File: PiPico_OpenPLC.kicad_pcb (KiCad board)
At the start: 2 copper layers, 155.6 x 86 mm, 196 parts, among them J1 5 Pin 3.5mm, J10 Conn_01x03_Male, J11 Conn_01x03_Male, J12 5 Pin 3.5mm, J2 5 Pin 3.5mm, J3 5 Pin 3.5mm, J4 5 Pin 3.5mm, J5 5 Pin 3.5mm, J6 5 Pin 3.5mm, J7 5 Pin 3.5mm, J8 5 Pin 3.5mm, J9 Conn_01x06_Male, K1 HF32F/xxx-Z, K2 HF32F/xxx-Z, K3 HF32F/xxx-Z, K4 HF32F/xxx-Z, Q1 MMBT2222A 1P, SW1 TS1187, U1 Pico, U10 ULN2803A, U11 LM2596S-12, U2 AMS1117-5.0, U3 LM4040DBZ-3, U4 LM358, U5 LM358, U6 LM358, U7 74HC14, U8 ULN2803A, U9 ULN2803A

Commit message: routed version
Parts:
- JP1, JP2, JP3, JP4, JP5, NT1, NT2, NT3, NT4, NT5, NT6: moved to B.Cu
- moved C11 242.3 mm to (38.6, 77.6), turned to 90 degrees
- moved JP3 238.9 mm to (42.1, 69.9), turned to 90 degrees
- moved D7 238.5 mm to (42.7, 44.1), turned to 90 degrees
- moved C1 237.4 mm to (38.6, 63.2), turned to 90 degrees
- moved C4 237.3 mm to (39.7, 80.4), turned to 180 degrees
- moved C3 237.0 mm to (39.7, 84.3), turned to -90 degrees
- moved C8 235.8 mm to (40.3, 77.6), turned to 90 degrees
- moved JP4 234.9 mm to (46.7, 55.6)
- moved D10 234.9 mm to (46.2, 44.1), turned to 90 degrees
- moved JP2 234.4 mm to (46.7, 58.5)
- moved D43 231.2 mm to (49.7, 44.1), turned to 90 degrees
- moved D9 230.9 mm to (45.6, 63.2), turned to -90 degrees
- moved C2 229.7 mm to (45.6, 67.1)
- moved F10 228.6 mm to (59.0, 36.5), turned to 180 degrees
- moved D44 227.7 mm to (53.2, 44.1), turned to 90 degrees
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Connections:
- net Vdrive renamed VPP
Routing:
- net GND: track 0.00 -> 898.8 mm, vias 0 -> 10
- net VCC: track 0.00 -> 298.8 mm, vias 0 -> 4
- net GNDA: track 0.00 -> 222.0 mm, vias 0 -> 6
- net VCCQ: track 0.00 -> 206.4 mm, vias 0 -> 2
- net VPP: track 0.00 -> 188.2 mm
- net +3V3: track 0.00 -> 171.9 mm, vias 0 -> 1
- net /PWMo0: track 0.00 -> 171.4 mm, vias 0 -> 2
- net VBUS: track 0.00 -> 141.5 mm, vias 0 -> 2
- net /Di0: track 0.00 -> 129.6 mm
- net /PWMo1: track 0.00 -> 121.4 mm, vias 0 -> 1
- net ADC_VREF: track 0.00 -> 116.6 mm, vias 0 -> 1
- net +12V: track 0.00 -> 103.8 mm, vias 0 -> 3
- net /Di7: track 0.00 -> 103.4 mm
- net /Di2: track 0.00 -> 103.3 mm, vias 0 -> 2
- net +5V: track 0.00 -> 93.6 mm, vias 0 -> 2
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
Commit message: snap
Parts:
- added C46: 50V 100nF X7R, Capacitor_SMD:C_0603_1608Metric, F.Cu at (109.7, 97.4)
- added C47: 50V 100nF X7R, Capacitor_SMD:C_0603_1608Metric, F.Cu at (78.2, 88.3)
- added C48: 50V 100nF X7R, Capacitor_SMD:C_0603_1608Metric, F.Cu at (119.9, 64.9)
- added D46: Red, LED_SMD:LED_0603_1608Metric, F.Cu at (49.7, 110.0)
- added D47: Red, LED_SMD:LED_0603_1608Metric, F.Cu at (46.2, 110.0)
- added D48: Red, LED_SMD:LED_0603_1608Metric, F.Cu at (42.7, 110.0)
- added D49: Red, LED_SMD:LED_0603_1608Metric, F.Cu at (39.2, 110.0)
- added J13: Conn_01x06_Male, Connector_PinHeader_2.54mm:PinHeader_1x06_P2.54mm_Vertical, F.Cu at (38.0, 97.6)
- added J14: 5 Pin 3.5mm, Connector_Phoenix_MC:PhoenixContact_MC_1,5_5-G-3.5_1x05_P3.50mm_Horizontal, F.Cu at (39.2, 114.8)
- added J15: Conn_01x06_Male, Connector_PinHeader_2.54mm:PinHeader_1x06_P2.54mm_Vertical, F.Cu at (183.8, 55.6)
- added J16: Conn_01x06_Male, Connector_PinHeader_2.54mm:PinHeader_1x06_P2.54mm_Vertical, F.Cu at (109.2, 73.8)
- added J17: Conn_01x06_Male, Connector_PinHeader_2.54mm:PinHeader_1x06_P2.54mm_Vertical, F.Cu at (109.2, 92.2)
- added J18: Conn_01x06_Male, Connector_PinHeader_2.54mm:PinHeader_1x06_P2.54mm_Vertical, F.Cu at (113.2, 61.1)
- added J19: Conn_01x06_Male, Connector_PinHeader_2.54mm:PinHeader_1x06_P2.54mm_Vertical, F.Cu at (113.2, 79.5)
- added J20: Conn_01x06_Male, Connector_PinHeader_2.54mm:PinHeader_1x06_P2.54mm_Vertical, F.Cu at (73.4, 43.2)
- added J21: Conn_01x06_Male, Connector_PinHeader_2.54mm:PinHeader_1x06_P2.54mm_Vertical, F.Cu at (148.2, 110.0)
- added J22: 5 Pin 3.5mm, Connector_Phoenix_MC:PhoenixContact_MC_1,5_5-G-3.5_1x05_P3.50mm_Horizontal, F.Cu at (148.2, 114.8)
- added JP8: SolderJumper_3_Bridged12, Connector_PinHeader_2.54mm:PinHeader_1x03_P2.54mm_Vertical, F.Cu at (139.9, 101.4)
- added NT7: NetTie_2, NetTie:NetTie-2_SMD_Pad0.5mm, B.Cu at (112.2, 97.4)
- added NT8: NetTie_2, NetTie:NetTie-2_SMD_Pad0.5mm, B.Cu at (121.4, 65.2)
- added NT9: NetTie_2, NetTie:NetTie-2_SMD_Pad0.5mm, B.Cu at (76.5, 80.0)
- added R45: 100k, Resistor_SMD:R_0603_1608Metric, F.Cu at (47.9, 110.0)
- added R46: 100k, Resistor_SMD:R_0603_1608Metric, F.Cu at (44.4, 110.0)
- added R47: 100k, Resistor_SMD:R_0603_1608Metric, F.Cu at (40.9, 110.0)
- added R48: 100k, Resistor_SMD:R_0603_1608Metric, F.Cu at (37.4, 110.0)
- added RN7: 470, Resistor_SMD:R_Array_Convex_4x0603, F.Cu at (50.8, 104.3)
- added U12: PCF8574, Package_SO:SOIC-16W_7.5x10.3mm_P1.27mm, F.Cu at (116.7, 101.4)
- added U15: PCF8574, Package_SO:SOIC-16W_7.5x10.3mm_P1.27mm, F.Cu at (126.9, 69.2)
- added U16: PCF8574, Package_SO:SOIC-16W_7.5x10.3mm_P1.27mm, F.Cu at (71.8, 84.3)
- J9: value Conn_01x06_Male -> 5 Pin 3.5mm; footprint Connector_PinHeader_2.54mm:PinHeader_1x06_P2.54mm_Vertical -> Connector_Phoenix_MC:PhoenixContact_MC_1,5_5-G-3.5_1x05_P3.50mm_Horizontal
- moved U10 62.5 mm to (46.7, 92.9), turned to 180 degrees
- moved C45 29.1 mm to (106.8, 105.1), turned to 180 degrees
- moved C44 28.1 mm to (106.8, 103.4), turned to 0 degrees
- moved J11 27.5 mm to (89.1, 88.1), turned to 90 degrees
- moved F8 26.4 mm to (106.8, 98.1), turned to -90 degrees
- moved RN6 25.1 mm to (107.4, 110.0), turned to 0 degrees
- moved D5 24.9 mm to (71.0, 63.4), turned to 90 degrees
- moved D4 24.7 mm to (75.0, 63.4), turned to 90 degrees
- moved J12 24.0 mm to (63.1, 114.8)
- moved J8 23.4 mm to (83.5, 114.8)
- moved C10 21.7 mm to (59.4, 87.7)
- moved C41 21.7 mm to (57.5, 87.7)
- moved D8 21.7 mm to (57.5, 79.5)
- moved F3 21.7 mm to (57.5, 84.7)
- moved C7 21.7 mm to (61.3, 85.9)
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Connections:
- F9 pad 1: VPP -> Net-(JP8-C)
- J9 pad 1: +3V3 -> Net-(J20-Pin_1)
- J9 pad 2: /SDA / UART Tx / SPI Rx -> Net-(J20-Pin_2)
- J9 pad 3: /SCL / UART Rx / SPI ~{CS} -> Net-(J20-Pin_3)
- J9 pad 4: /SPI SCK -> Net-(J20-Pin_4)
- J9 pad 5: /SPI Tx -> Net-(J20-Pin_5)
- R14 pad 1: GNDA -> GND
- R15 pad 1: GNDA -> GND
- U1 pad 1: /SDA / UART Tx / SPI Rx -> /UART0_TX
- U1 pad 10: /Di1 -> unconnected-(U1-GPIO7-Pad10)
- U1 pad 11: /Di2 -> /UART1_TX
- U1 pad 12: /Di3 -> /UART1_RX
- U1 pad 14: /Di4 -> unconnected-(U1-GPIO10-Pad14)
- U1 pad 15: /Di5 -> unconnected-(U1-GPIO11-Pad15)
- U1 pad 16: /Di6 -> /SPI1_RX
- U1 pad 17: /Di7 -> /SPI1_CSn
- U1 pad 19: /Do0 -> /SPI1_SCK
- U1 pad 2: /SCL / UART Rx / SPI ~{CS} -> /UART0_RX
- U1 pad 20: /Do1 -> /SPI1_TX
- U1 pad 21: /Do2 -> /SPI0_RX
- U1 pad 22: /Do3 -> /SPI0_CSn
- U1 pad 24: /Do4 -> /SPI0_SCK
- U1 pad 25: /Do5 -> /SPI0_TX
- U1 pad 26: /Do6 -> /PWMo0
- U1 pad 27: /Do7 -> /PWMo1
- U1 pad 4: /SPI SCK -> /I2C1_SDA
- U1 pad 5: /SPI Tx -> /I2C1_SCL
- U1 pad 6: /PWMo1 -> /I2C0_SDA
- U1 pad 7: /PWMo0 -> /I2C0_SCL
- U1 pad 9: /Di0 -> unconnected-(U1-GPIO6-Pad9)
- U10 pad 1: GND -> /Digital_Output/Do15
- U10 pad 11: /Digital_Output/z0 -> /Digital_Output/Xo8
- U10 pad 12: /Digital_Output/z1 -> /Digital_Output/Xo9
- U10 pad 13: /Digital_Output/z2 -> /Digital_Output/Xo10
- U10 pad 14: /Digital_Output/z3 -> /Digital_Output/Xo11
- U10 pad 15: unconnected-(U10-O4-Pad15) -> /Digital_Output/z0
- U10 pad 16: unconnected-(U10-O3-Pad16) -> /Digital_Output/z1
- U10 pad 17: unconnected-(U10-O2-Pad17) -> /Digital_Output/z2
- U10 pad 18: unconnected-(U10-O1-Pad18) -> /Digital_Output/z3
- U10 pad 2: GND -> /Digital_Output/Do14
- U10 pad 3: GND -> /Digital_Output/Do13
- U10 pad 4: GND -> /Digital_Output/Do12
- U10 pad 5: /Do3 -> /Digital_Output/Do11
- U10 pad 6: /Do2 -> /Digital_Output/Do10
- U10 pad 7: /Do1 -> /Digital_Output/Do9
- U10 pad 8: /Do0 -> /Digital_Output/Do8
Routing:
- net GND: track 898.8 -> 183.3 mm, vias 10 -> 55
- net VDC: track 45.3 -> 291.3 mm, vias 0 -> 3
- net +3V3: track 171.9 -> 315.1 mm
- net /I2C0_SDA: track 0.00 -> 125.2 mm, vias 0 -> 3
- net /I2C0_SCL: track 0.00 -> 121.4 mm, vias 0 -> 3
- net GNDA: track 222.0 -> 114.9 mm, vias 6 -> 21
- net VCC: track 298.8 -> 405.1 mm, vias 4 -> 5
- net Net-(J14-Pin_5): track 49.6 -> 154.4 mm, vias 1 -> 2
- net /UART0_TX: track 0.00 -> 80.7 mm
- net /UART0_RX: track 0.00 -> 79.1 mm
- net /Di0: track 129.6 -> 54.9 mm
- net /Di7: track 103.4 -> 34.0 mm
- net /PWMo0: track 171.4 -> 106.8 mm, vias 2 -> 0
- net /Do0: track 77.8 -> 13.4 mm, vias 1 -> 0
- net /Di2: track 103.3 -> 39.7 mm, vias 2 -> 0
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- added copper zone on In1.Cu, net GND
- added copper zone on In1.Cu, net GNDA
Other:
- copper layers 2 -> 4

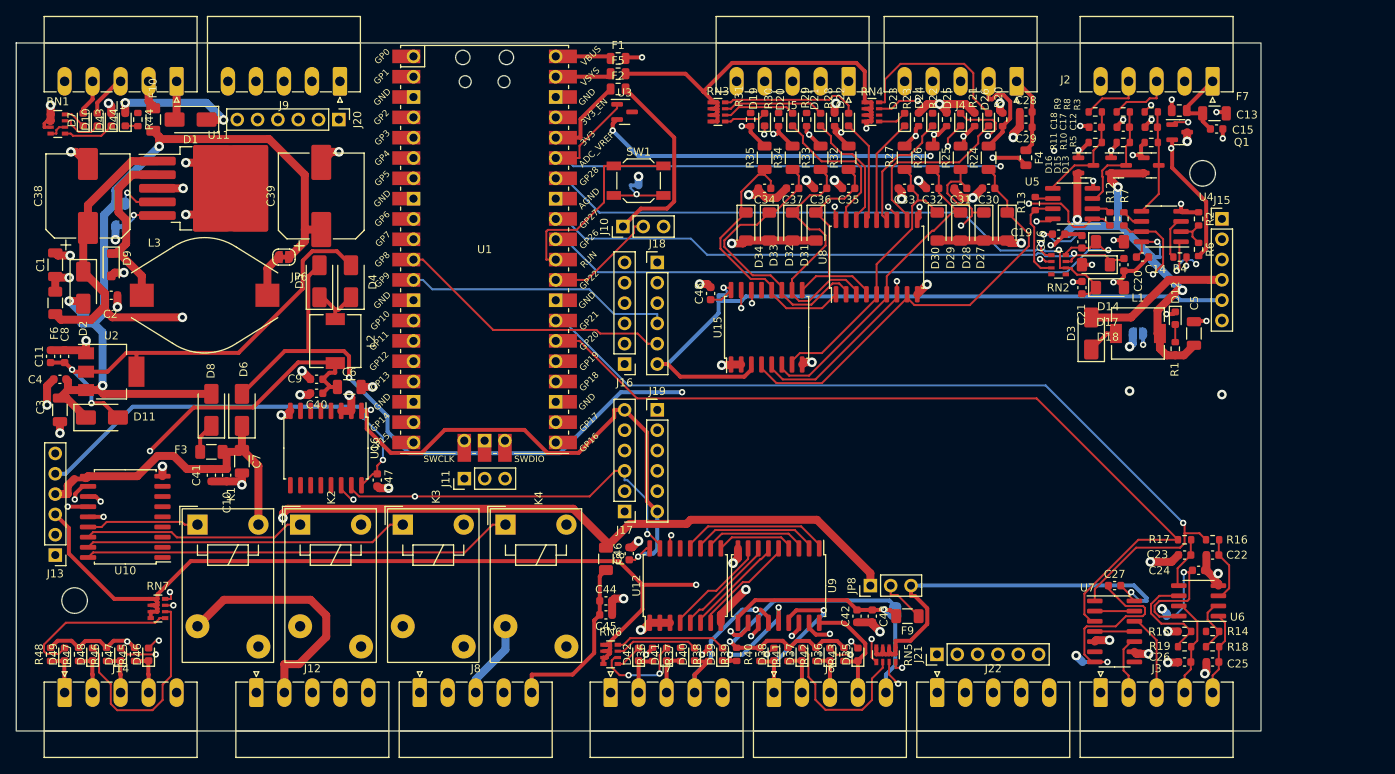
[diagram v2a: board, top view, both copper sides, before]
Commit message: Preparation for future use.
Reworked to use i2c bus expanders.
added sketch for add-on boards.
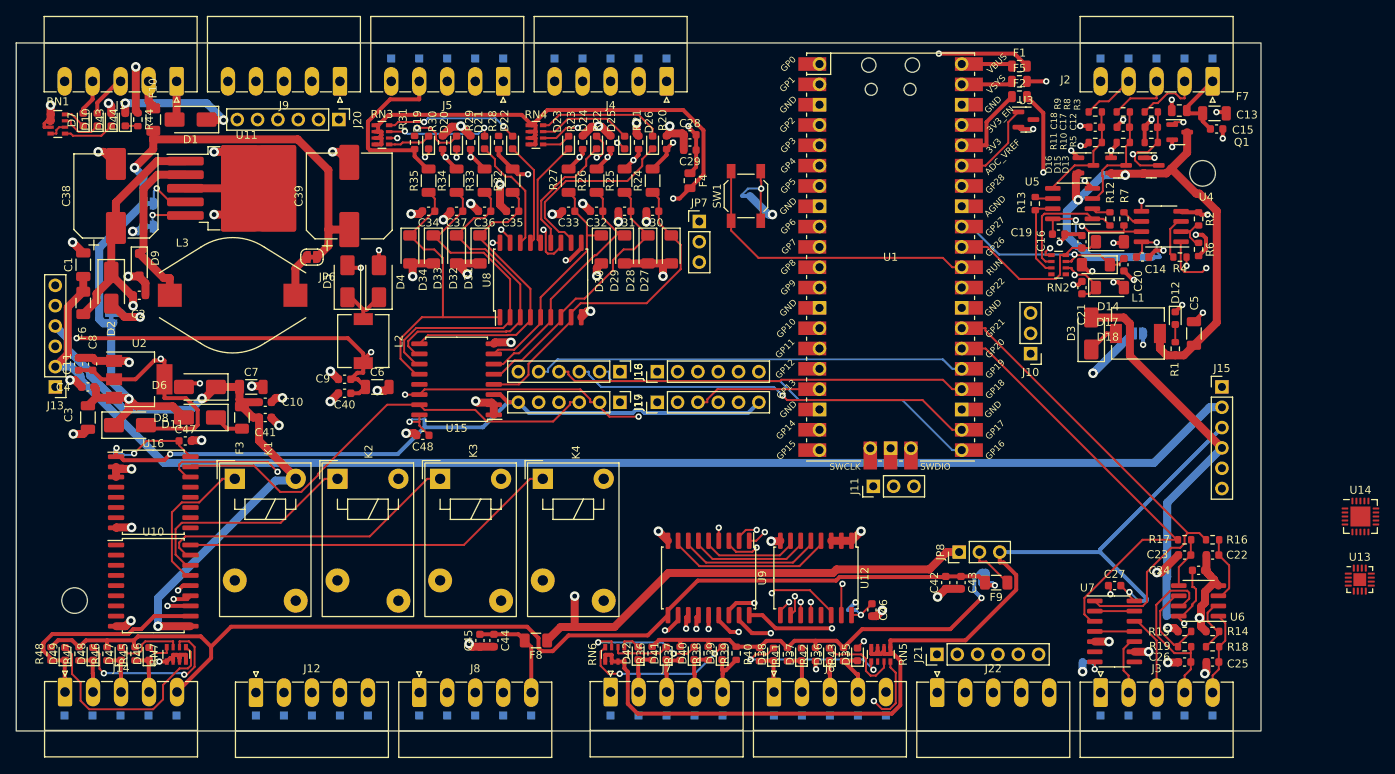
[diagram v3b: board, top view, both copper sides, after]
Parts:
- added JP7: 5V < V_{I} > V_{DC}, Connector_PinHeader_2.54mm:PinHeader_1x03_P2.54mm_Vertical, F.Cu at (118.5, 55.9)
- added TP1: X_{o}1, TestPoint:TestPoint_Pad_1.0x1.0mm, B.Cu at (114.4, 117.7)
- added TP10: X_{o}9, TestPoint:TestPoint_Pad_1.0x1.0mm, B.Cu at (42.7, 117.7)
- added TP11: X_{o}10, TestPoint:TestPoint_Pad_1.0x1.0mm, B.Cu at (46.2, 117.7)
- added TP12: X_{o}11, TestPoint:TestPoint_Pad_1.0x1.0mm, B.Cu at (49.7, 117.7)
- added TP13: X_{o}0, TestPoint:TestPoint_Pad_1.0x1.0mm, B.Cu at (110.9, 117.7)
- added TP14: GND, TestPoint:TestPoint_Pad_1.0x1.0mm, B.Cu at (63.1, 117.7)
- added TP15: V_{O}, TestPoint:TestPoint_Pad_1.0x1.0mm, B.Cu at (53.2, 117.7)
- added TP16: V_{O}, TestPoint:TestPoint_Pad_1.0x1.0mm, B.Cu at (141.8, 117.7)
- added TP17: GND, TestPoint:TestPoint_Pad_1.0x1.0mm, B.Cu at (107.4, 117.7)
- added TP18: NO4, TestPoint:TestPoint_Pad_1.0x1.0mm, B.Cu at (94.0, 117.7)
- added TP19: C4, TestPoint:TestPoint_Pad_1.0x1.0mm, B.Cu at (90.5, 117.7)
- added TP2: X_{o}2, TestPoint:TestPoint_Pad_1.0x1.0mm, B.Cu at (117.9, 117.7)
- added TP20: NO3, TestPoint:TestPoint_Pad_1.0x1.0mm, B.Cu at (87.0, 117.7)
- added TP21: C3, TestPoint:TestPoint_Pad_1.0x1.0mm, B.Cu at (83.5, 117.7)
- added TP22: NO2, TestPoint:TestPoint_Pad_1.0x1.0mm, B.Cu at (77.1, 117.7)
- added TP23: C2, TestPoint:TestPoint_Pad_1.0x1.0mm, B.Cu at (73.6, 117.7)
- added TP24: NO1, TestPoint:TestPoint_Pad_1.0x1.0mm, B.Cu at (70.1, 117.7)
- added TP25: C1, TestPoint:TestPoint_Pad_1.0x1.0mm, B.Cu at (66.6, 117.7)
- added TP26: V_{I}, TestPoint:TestPoint_Pad_1.0x1.0mm, B.Cu at (114.4, 35.6)
- added TP27: GND, TestPoint:TestPoint_Pad_1.0x1.0mm, B.Cu at (80.0, 35.6)
- added TP28: GND, TestPoint:TestPoint_Pad_1.0x1.0mm, B.Cu at (168.7, 117.7)
- added TP29: A_{o}0, TestPoint:TestPoint_Pad_1.0x1.0mm, B.Cu at (182.7, 117.7)
- added TP3: V_{DC}, TestPoint:TestPoint_Pad_1.0x1.0mm, B.Cu at (97.5, 117.7)
- added TP30: A_{o}1, TestPoint:TestPoint_Pad_1.0x1.0mm, B.Cu at (179.2, 117.7)
- added TP31: PWM_{o}0, TestPoint:TestPoint_Pad_1.0x1.0mm, B.Cu at (175.7, 117.7)
- added TP32: X_{i}7, TestPoint:TestPoint_Pad_1.0x1.0mm, B.Cu at (83.5, 35.6)
- added TP33: X_{i}6, TestPoint:TestPoint_Pad_1.0x1.0mm, B.Cu at (87.0, 35.6)
- added TP34: X_{i}5, TestPoint:TestPoint_Pad_1.0x1.0mm, B.Cu at (90.5, 35.6)
- added TP35: X_{i}4, TestPoint:TestPoint_Pad_1.0x1.0mm, B.Cu at (94.0, 35.6)
- added TP36: X_{i}3, TestPoint:TestPoint_Pad_1.0x1.0mm, B.Cu at (100.4, 35.6)
- added TP37: X_{i}2, TestPoint:TestPoint_Pad_1.0x1.0mm, B.Cu at (103.9, 35.6)
- added TP38: X_{i}1, TestPoint:TestPoint_Pad_1.0x1.0mm, B.Cu at (107.4, 35.6)
- added TP39: X_{i}0, TestPoint:TestPoint_Pad_1.0x1.0mm, B.Cu at (110.9, 35.6)
- added TP4: X_{o}3, TestPoint:TestPoint_Pad_1.0x1.0mm, B.Cu at (121.4, 117.7)
- added TP40: PWM_{o}1, TestPoint:TestPoint_Pad_1.0x1.0mm, B.Cu at (172.2, 117.7)
- added TP41: V_{Ana}, TestPoint:TestPoint_Pad_1.0x1.0mm, B.Cu at (182.7, 35.6)
- added TP42: A_{i}0, TestPoint:TestPoint_Pad_1.0x1.0mm, B.Cu at (179.2, 35.6)
- added TP43: A_{i}1, TestPoint:TestPoint_Pad_1.0x1.0mm, B.Cu at (175.7, 35.6)
- added TP44: A_{i}2, TestPoint:TestPoint_Pad_1.0x1.0mm, B.Cu at (172.2, 35.6)
- added TP45: GND_{Ana}, TestPoint:TestPoint_Pad_1.0x1.0mm, B.Cu at (168.7, 35.6)
- added TP5: X_{o}4, TestPoint:TestPoint_Pad_1.0x1.0mm, B.Cu at (127.8, 117.7)
- added TP6: X_{o}5, TestPoint:TestPoint_Pad_1.0x1.0mm, B.Cu at (131.3, 117.7)
- added TP7: X_{o}6, TestPoint:TestPoint_Pad_1.0x1.0mm, B.Cu at (134.8, 117.7)
- added TP8: X_{o}7, TestPoint:TestPoint_Pad_1.0x1.0mm, B.Cu at (138.3, 117.7)
- added TP9: X_{o}8, TestPoint:TestPoint_Pad_1.0x1.0mm, B.Cu at (39.2, 117.7)
- added U13: PCF8574, Package_DFN_QFN:WQFN-16-1EP_3x3mm_P0.5mm_EP1.6x1.6mm, F.Cu at (201.1, 100.7)
- added U14: ULN2803A, Package_DFN_QFN:QFN-20-1EP_4x4mm_P0.5mm_EP2.5x2.5mm, F.Cu at (201.1, 92.8)
- JP1: value Jumper_2_Open -> GND <-> GND_{Ana}
- JP8: value SolderJumper_3_Bridged12 -> 5V < V_{IO} > V_{DC}
- moved J10 53.4 mm to (159.9, 72.5), turned to 180 degrees
- moved J11 51.1 mm to (140.2, 89.0)
- moved U1 50.8 mm to (142.4, 60.4)
- moved F1 50.2 mm to (158.5, 36.5)
- moved F2 50.2 mm to (158.5, 40.3)
- moved F5 50.2 mm to (158.5, 38.4)
- moved U3 50.2 mm to (159.3, 43.2)
- moved J4 43.8 mm to (114.4, 38.4)
- moved J5 43.2 mm to (94.0, 38.4)
- moved D27 42.1 mm to (115.0, 59.4)
- moved D30 42.1 mm to (106.2, 59.4)
- moved D34 42.1 mm to (82.3, 59.4)
- moved RN3 42.1 mm to (78.8, 45.1)
- moved C28 42.1 mm to (117.3, 45.1)
- moved C29 42.1 mm to (117.3, 47.0)
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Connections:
- F4 pad 2: VCC -> Net-(JP7-C)
- R45 pad 2: Net-(J14-Pin_5) -> Net-(JP5-B)
- R46 pad 2: Net-(J14-Pin_5) -> Net-(JP5-B)
- R47 pad 2: Net-(J14-Pin_5) -> Net-(JP5-B)
- R48 pad 2: Net-(J14-Pin_5) -> Net-(JP5-B)
- U10 pad 1: /Digital_Output/Do15 -> /Do15
- U10 pad 2: /Digital_Output/Do14 -> /Do14
- U10 pad 3: /Digital_Output/Do13 -> /Do13
- U10 pad 4: /Digital_Output/Do12 -> /Do12
- U10 pad 5: /Digital_Output/Do11 -> /Do11
- U10 pad 6: /Digital_Output/Do10 -> /Do10
- U10 pad 7: /Digital_Output/Do9 -> /Do9
- U10 pad 8: /Digital_Output/Do8 -> /Do8
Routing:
- net VDC: track 291.3 -> 224.9 mm, vias 3 -> 2
- net GNDA: track 114.9 -> 57.9 mm, vias 21 -> 22
- net /ADC0: track 78.5 -> 21.8 mm, vias 1 -> 0
- net VCC: track 405.1 -> 461.3 mm, vias 5 -> 6
- net /ADC1: track 76.0 -> 24.3 mm
- net /PWMo0: track 106.8 -> 55.3 mm
- net ADC_VREF: track 97.1 -> 46.1 mm, vias 2 -> 1
- net /PWMo1: track 109.8 -> 60.1 mm, vias 1 -> 0
- net /ADC2: track 77.0 -> 34.0 mm
- net VCCQ: track 228.2 -> 269.8 mm, vias 1 -> 2
- net /I2C0_SDA: track 125.2 -> 163.5 mm, vias 3 -> 1
- net /SPI0_SCK: track 14.0 -> 51.6 mm
- net /SPI0_TX: track 17.8 -> 54.2 mm
- net /SPI0_CSn: track 16.6 -> 51.0 mm, vias 0 -> 1
- net /SPI0_RX: track 16.6 -> 49.8 mm
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
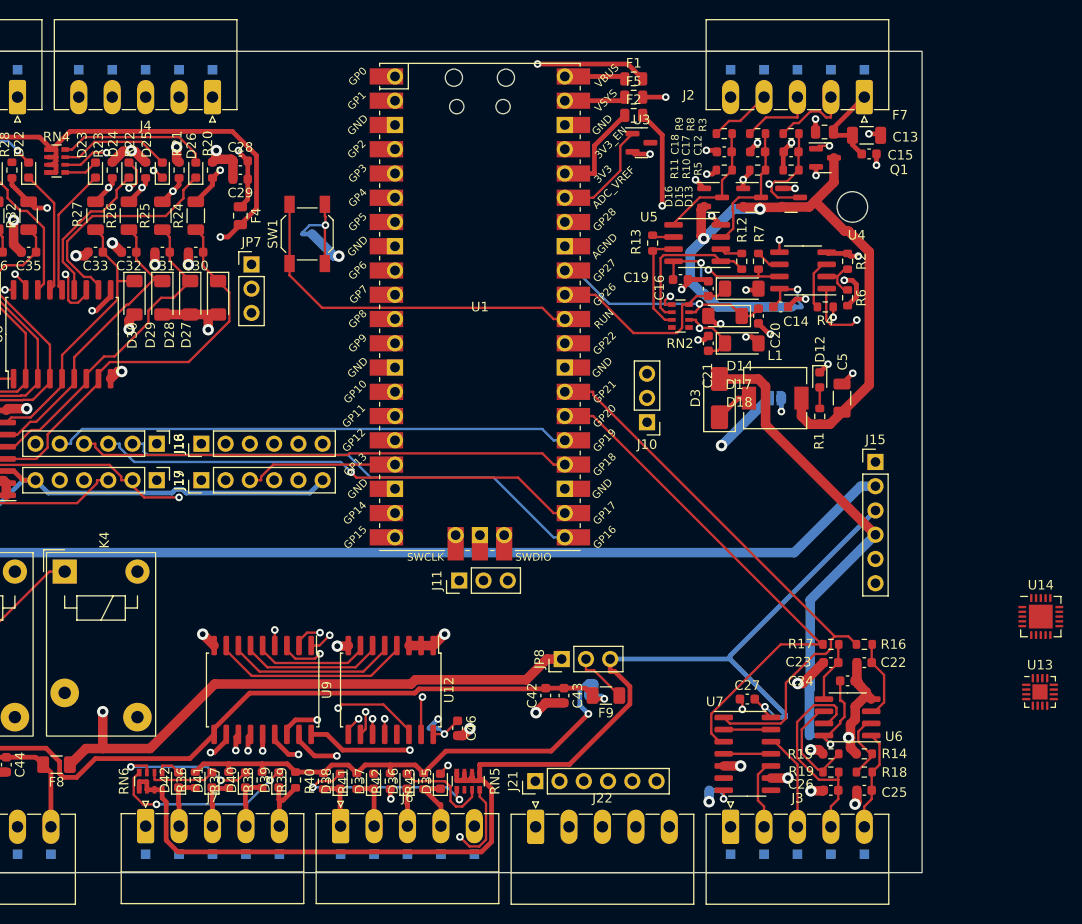
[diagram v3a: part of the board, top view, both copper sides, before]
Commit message: Added Submodule, changed Ports to i2c
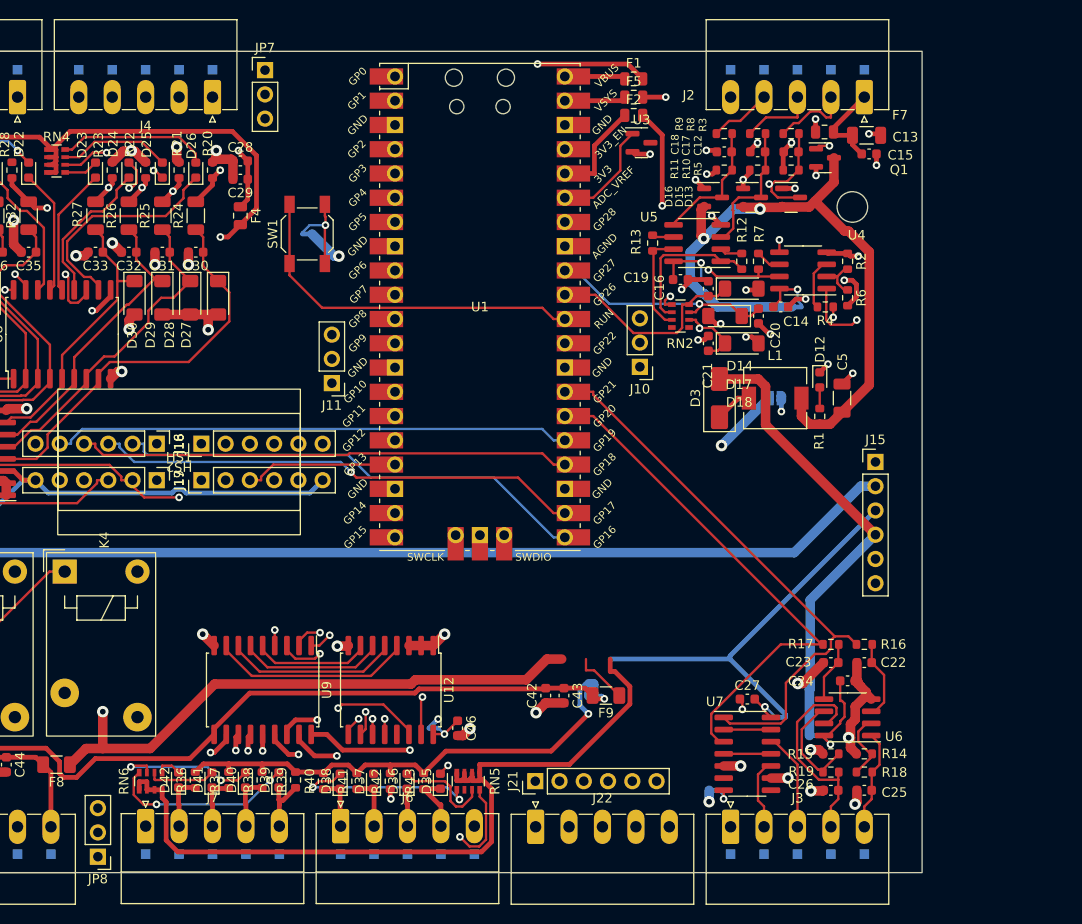
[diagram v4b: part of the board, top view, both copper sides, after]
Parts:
- removed U13: PCF8574, Package_DFN_QFN:WQFN-16-1EP_3x3mm_P0.5mm_EP1.6x1.6mm
- removed U14: ULN2803A, Package_DFN_QFN:QFN-20-1EP_4x4mm_P0.5mm_EP2.5x2.5mm
- added HS1, HS2: Submodule, Project:Submodule, F.Cu at (110.9, 76.6)
- moved JP8 52.8 mm to (102.4, 117.9), turned to 180 degrees
- moved J11 24.6 mm to (126.9, 68.4), turned to 180 degrees
- moved JP7 20.4 mm to (119.9, 35.6)
- moved J10 5.85 mm to (159.2, 66.7)
